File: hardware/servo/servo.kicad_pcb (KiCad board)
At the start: 2 copper layers, 100 x 62 mm, 90 parts, among them J1 Midi In, J2 Midi Thru, J3 NeoPixel, J4 Power, J6 I2C0, J7 I2C1, M1 Motor_Servo, M10 Motor_Servo, M11 Motor_Servo, M12 Motor_Servo, M13 Motor_Servo, M14 Motor_Servo, M15 Motor_Servo, M16 Motor_Servo, M2 Motor_Servo, M3 Motor_Servo, M4 Motor_Servo, M5 Motor_Servo, M6 Motor_Servo, M7 Motor_Servo, M8 Motor_Servo, M9 Motor_Servo, Q1 BSS138, Q2 BSS138, Q3 TSM680P06, SW1 Reset, U1 6N138, U2 74AHC1G125, U3 74AHC1G125, U4 Raspberry Pi Pico, U5 AZ1117-5.0, U6 AZ1117-5.0, U7 GS8331

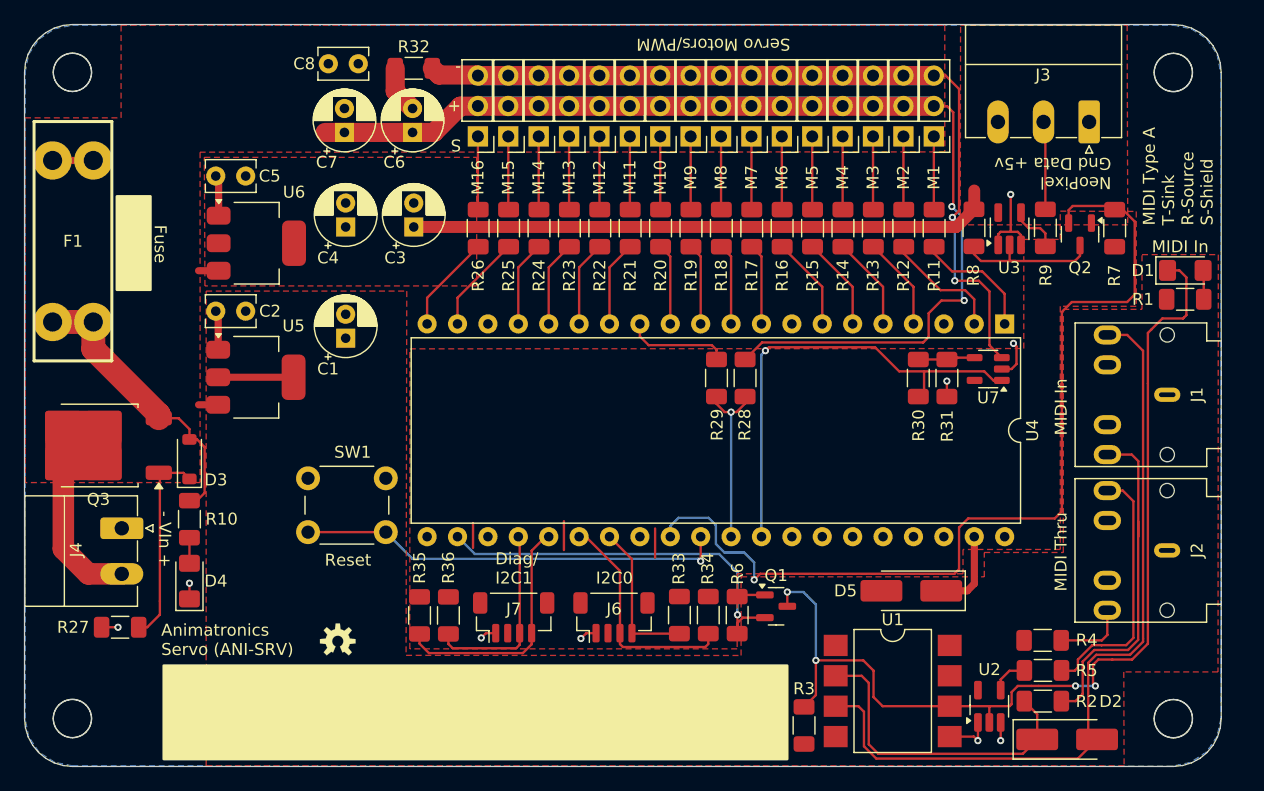
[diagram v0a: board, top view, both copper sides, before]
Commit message: Rev 1.1: - Update to latest KiCad - Fixed short in servo board - Updates to right-angle diag connector on servo boards - Fixed microproc footprint on diag board - Flipped I2C connector to top of diag board - Pass all ERC and DRC checks, add exclusions
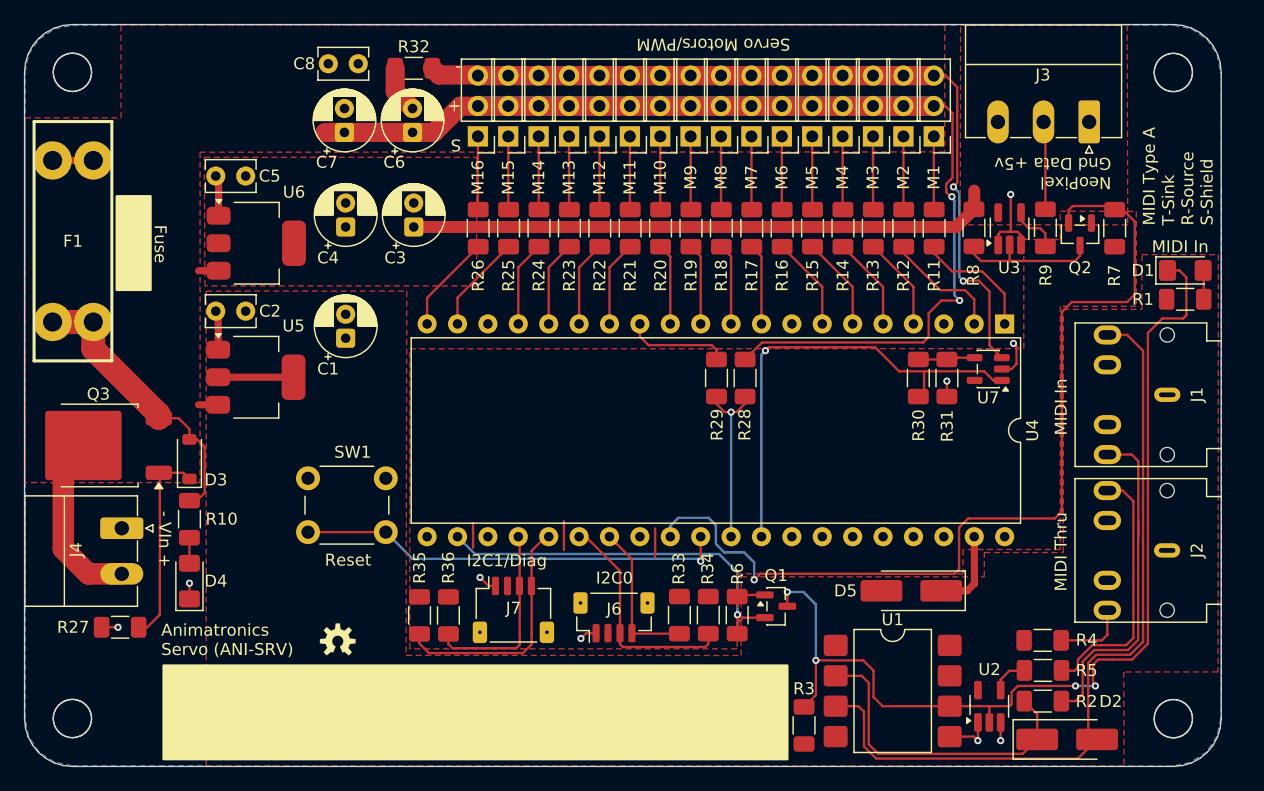
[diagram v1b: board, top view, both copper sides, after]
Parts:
- J7: footprint Connector_JST:JST_SH_BM04B-SRSS-TB_1x04-1MP_P1.00mm_Vertical -> Connector_JST:JST_SH_SM04B-SRSS-TB_1x04-1MP_P1.00mm_Horizontal
- moved J7 0.62 mm to (130.8, 107.2)
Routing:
- net Net-(M1--): track 108.5 -> 107.9 mm
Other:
- board text added: "ANI-SRV, Rev 1.1 Sparky Bobo Designs"
- board text added: "I2C1/Diag"
- board text removed: "ANI-SRV, Rev 1.0 Sparky Bobo Designs"
- board text removed: "Diag/ I2C1"
